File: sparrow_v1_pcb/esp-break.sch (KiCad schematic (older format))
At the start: 23 parts, among them J1 Conn_02x03_Odd_Even, Q1 BSS138, Q2 BSS138, SW1 SW_Push, U1 ESP32-WROOM-32D, U2 AP1117-33

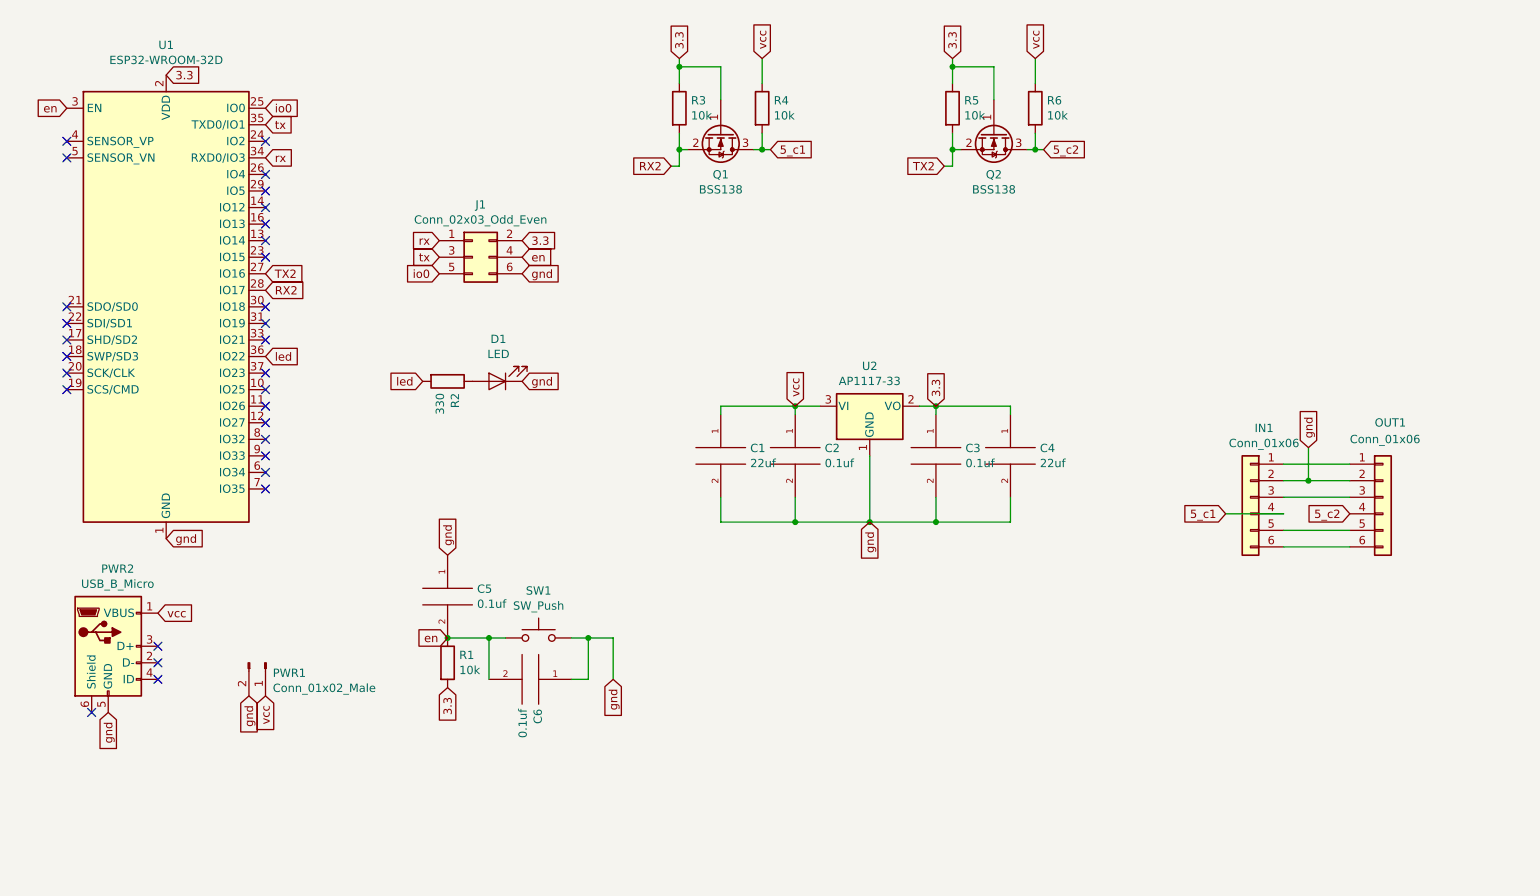
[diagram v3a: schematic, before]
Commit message: Added buck converter and routing
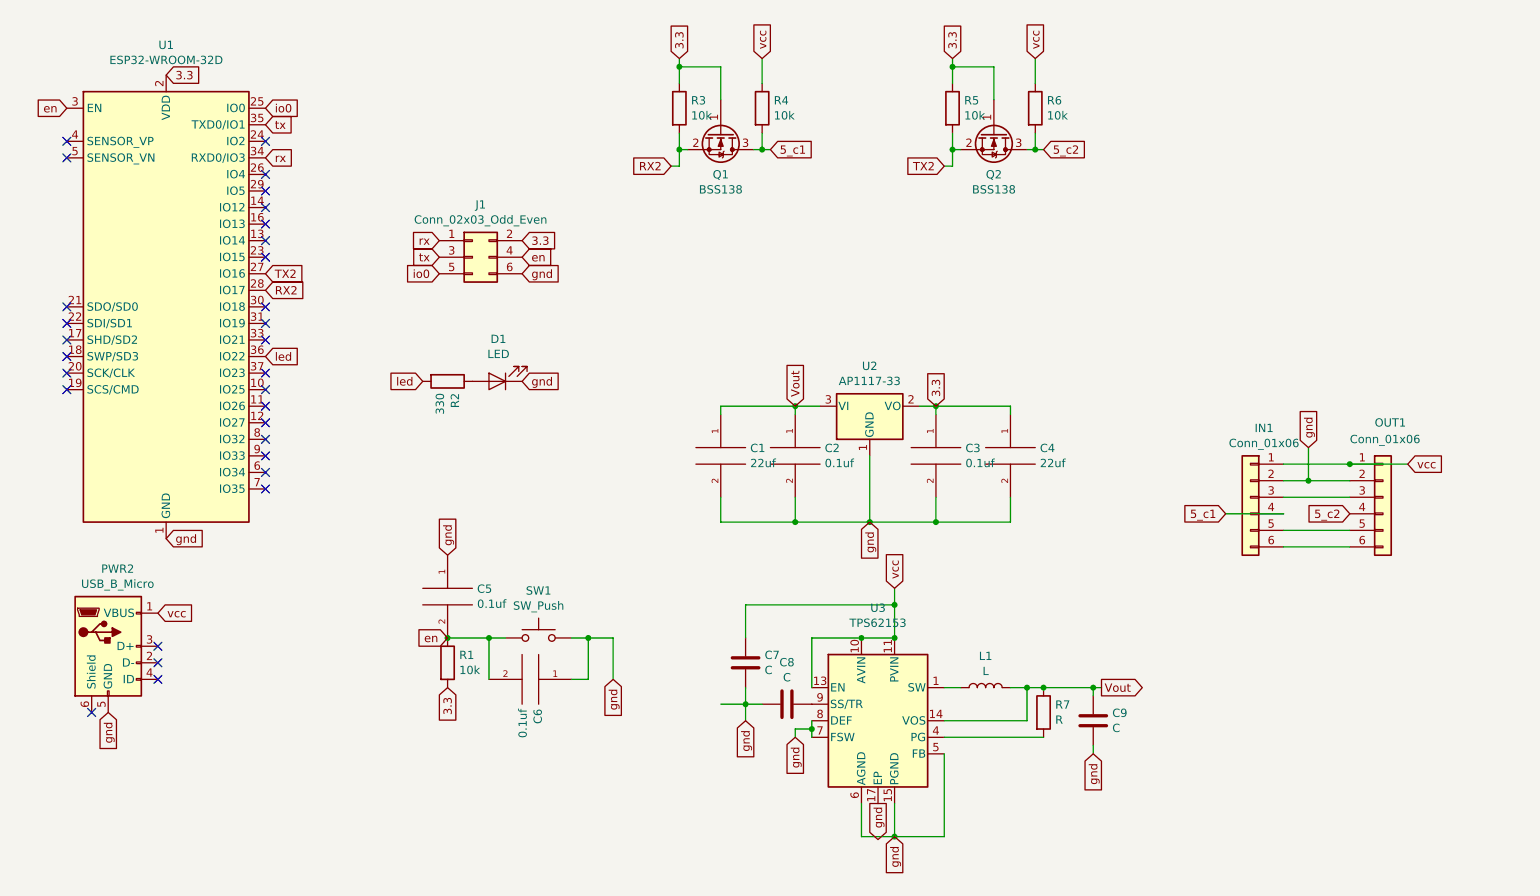
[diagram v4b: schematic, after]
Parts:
- removed PWR1: Conn_01x02_Male, Connector_PinHeader_2.54mm:PinHeader_1x02_P2.54mm_Vertical, symbol Connector:Conn_01x02_Male
- added C7: C, Capacitor_SMD:C_1210_3225Metric, symbol Device:C
- added C8: C, Capacitor_SMD:C_0201_0603Metric, symbol Device:C
- added C9: C, Capacitor_SMD:C_0805_2012Metric, symbol Device:C
- added L1: L, Inductor_SMD:L_Coilcraft_XxL4020, symbol Device:L
- added R7: R, Resistor_SMD:R_0603_1608Metric, symbol Device:R
- added U3: TPS62153, Package_DFN_QFN:VQFN-16-1EP_3x3mm_P0.5mm_EP1.68x1.68mm_ThermalVias, symbol Regulator_Switching:TPS62153
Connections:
- net gnd: now also C7.2, C8.2, C9.2, U3.15 (PGND), U3.16 (PGND), U3.17 (EP), U3.5 (FB), U3.6 (AGND), U3.7 (FSW), U3.8 (DEF)
- net vcc: now also IN1.1 (Pin_1), OUT1.1 (Pin_1), C7.1, U3.10 (AVIN), U3.11 (PVIN), U3.12 (PVIN), U3.13 (EN); no longer C1.1, C2.1, U2.3 (VI)
- new net: L1.1, U3.1 (SW), U3.2 (SW), U3.3 (SW)
- new net: R7.2, U3.4 (PG)
- new net: C8.1, U3.9 (SS/TR)
- new net Vout: C1.1, C2.1, C9.1, L1.2, R7.1, U2.3 (VI), U3.14 (VOS)
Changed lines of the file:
@@
 gnd
 Text GLabel 6400 2800 1    50   Input ~ 0
-vcc
+Vout
 Text GLabel 2600 800  2    50   Input ~ 0
 3.3
@@
 	9350 3350 9750 3350
 Text GLabel 9500 3050 1    50   Input ~ 0
-gnd
-$Comp
-L Connector:Conn_01x02_Male PWR1
-U 1 1 5DCB9F6F
-P 3200 4350
-F 0 "PWR1" V 3262 4394 50  0000 L CNN
-F 1 "Conn_01x02_Male" V 3353 4394 50  0000 L CNN
-F 2 "Connector_PinHeader_2.54mm:PinHeader_1x02_P2.54mm_Vertical" H 3200 4350 50  0001 C CNN
-F 3 "~" H 3200 4350 50  0001 C CNN
-	1    3200 4350
-	0    1    1    0
-$EndComp
-Text GLabel 3200 4550 3    50   Input ~ 0
-vcc
-Text GLabel 3100 4550 3    50   Input ~ 0
 gnd
 $Comp
@@
 NoConn ~ 2000 2600
 NoConn ~ 2000 2700
+$Comp
+L Regulator_Switching:TPS62153 U3
+U 1 1 5F00BF3A
+P 6900 4700
+F 0 "U3" H 6900 5381 50  0000 C CNN
+F 1 "TPS62153" H 6900 5290 50  0000 C CNN
+F 2 "Package_DFN_QFN:VQFN-16-1EP_3x3mm_P0.5mm_EP1.68x1.68mm_ThermalVias" H 7050 4250 50  0001 L CNN
+F 3 "http://www.ti.com/lit/ds/symlink/TPS62150.pdf" H 6900 4700 50  0001 C CNN
+	1    6900 4700
+	1    0    0    -1
+$EndComp
+Text GLabel 7000 3900 1    50   Input ~ 0
+vcc
+Wire Wire Line
+	6500 4500 6500 4200
+Wire Wire Line
+	6500 4200 6800 4200
+Wire Wire Line
+	6800 4200 7000 4200
+Connection ~ 6800 4200
+Wire Wire Line
+	7000 4200 7000 4000
+Connection ~ 7000 4200
+$Comp
+L Device:C C8
+U 1 1 5F0139AE
+P 6350 4600
+F 0 "C8" V 6098 4600 50  0000 C CNN
+F 1 "C" V 6189 4600 50  0000 C CNN
+F 2 "Capacitor_SMD:C_0201_0603Metric" H 6388 4450 50  0001 C CNN
+F 3 "~" H 6350 4600 50  0001 C CNN
+	1    6350 4600
+	0    1    1    0
+$EndComp
+Wire Wire Line
+	6200 4600 6100 4600
+Text GLabel 6100 4700 3    50   Input ~ 0
+gnd
+Wire Wire Line
+	6100 4700 6100 4600
+Connection ~ 6100 4600
+Wire Wire Line
+	6100 4600 5950 4600
+$Comp
+L Device:C C7
+U 1 1 5F0181AC
+P 6100 4350
+F 0 "C7" H 6215 4396 50  0000 L CNN
+F 1 "C" H 6215 4305 50  0000 L CNN
+F 2 "Capacitor_SMD:C_1210_3225Metric" H 6138 4200 50  0001 C CNN
+F 3 "~" H 6100 4350 50  0001 C CNN
+	1    6100 4350
+	1    0    0    -1
+$EndComp
+Wire Wire Line
+	6100 4500 6100 4600
+Wire Wire Line
+	6100 4200 6100 4000
+Wire Wire Line
+	6100 4000 7000 4000
+Connection ~ 7000 4000
+Wire Wire Line
+	7000 4000 7000 3900
+Wire Wire Line
+	6500 4700 6500 4750
+Wire Wire Line
+	6500 4750 6400 4750
+Wire Wire Line
+	6400 4750 6400 4800
+Connection ~ 6500 4750
+Wire Wire Line
+	6500 4750 6500 4800
+Text GLabel 6400 4800 3    50   Input ~ 0
+gnd
+Wire Wire Line
+	6800 5200 6800 5400
+Wire Wire Line
+	6800 5400 7000 5400
+Wire Wire Line
+	7000 5400 7000 5200
+Wire Wire Line
+	7300 4900 7300 5400
+Wire Wire Line
+	7300 5400 7000 5400
+Connection ~ 7000 5400
+Text GLabel 7000 5400 3    50   Input ~ 0
+gnd
+Wire Wire Line
+	7300 4700 7800 4700
+Wire Wire Line
+	7800 4700 7800 4500
+$Comp
+L Device:R R7
+U 1 1 5F02689D
+P 7900 4650
+F 0 "R7" H 7970 4696 50  0000 L CNN
+F 1 "R" H 7970 4605 50  0000 L CNN
+F 2 "Resistor_SMD:R_0603_1608Metric" V 7830 4650 50  0001 C CNN
+F 3 "~" H 7900 4650 50  0001 C CNN
+	1    7900 4650
+	1    0    0    -1
+$EndComp
+Wire Wire Line
+	7300 4800 7900 4800
+Wire Wire Line
+	7800 4500 7900 4500
+Wire Wire Line
+	7900 4500 8200 4500
+Connection ~ 7900 4500
+$Comp
+L Device:C C9
+U 1 1 5F02D11A
+P 8200 4700
+F 0 "C9" H 8315 4746 50  0000 L CNN
+F 1 "C" H 8315 4655 50  0000 L CNN
+F 2 "Capacitor_SMD:C_0805_2012Metric" H 8238 4550 50  0001 C CNN
+F 3 "~" H 8200 4700 50  0001 C CNN
+	1    8200 4700
+	1    0    0    -1
+$EndComp
+Wire Wire Line
+	8200 4500 8200 4550
+Text GLabel 8200 4900 3    50   Input ~ 0
+gnd
+Wire Wire Line
+	8200 4850 8200 4900
+$Comp
+L Device:L L1
+U 1 1 5F032225
+P 7550 4500
+F 0 "L1" V 7740 4500 50  0000 C CNN
+F 1 "L" V 7649 4500 50  0000 C CNN
+F 2 "Inductor_SMD:L_Coilcraft_XxL4020" H 7550 4500 50  0001 C CNN
+F 3 "~" H 7550 4500 50  0001 C CNN
+	1    7550 4500
+	0    -1   -1   0
+$EndComp
+Wire Wire Line
+	7300 4500 7400 4500
+Wire Wire Line
+	7700 4500 7800 4500
+Connection ~ 7800 4500
+Text GLabel 8250 4500 2    50   Output ~ 0
+Vout
+Wire Wire Line
+	8200 4500 8250 4500
+Connection ~ 8200 4500
+Text GLabel 6900 5200 3    50   Output ~ 0
+gnd
+Text GLabel 10100 3150 2    50   Input ~ 0
+vcc
+Wire Wire Line
+	9750 3150 10100 3150
+Connection ~ 9750 3150
 $EndSCHEMATC

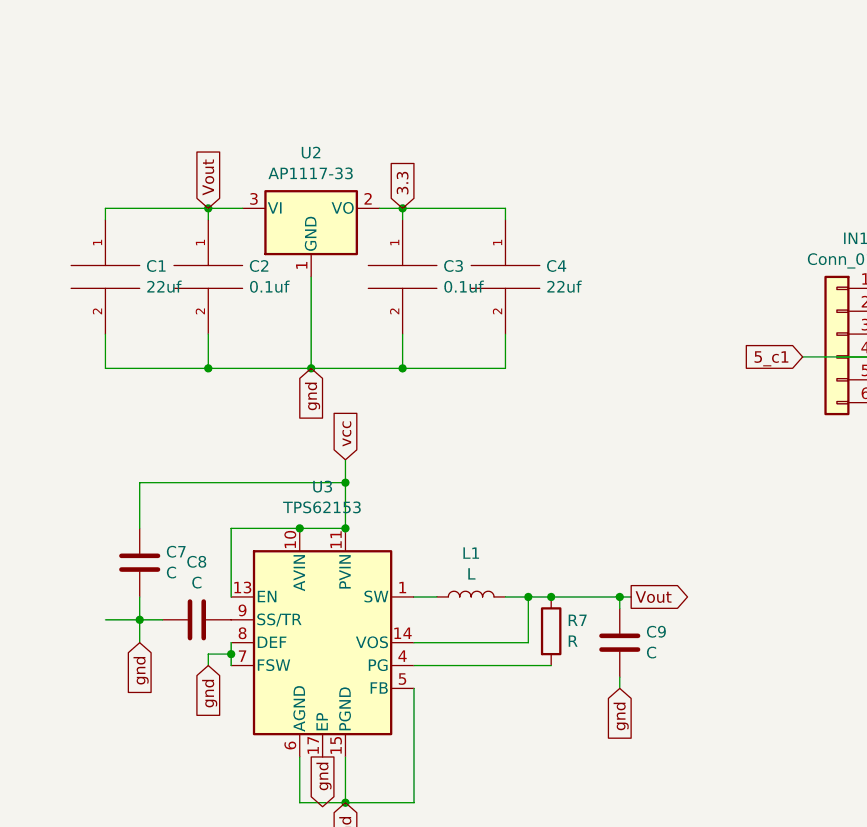
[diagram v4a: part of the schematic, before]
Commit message: added new component to schematic: LDO from ST
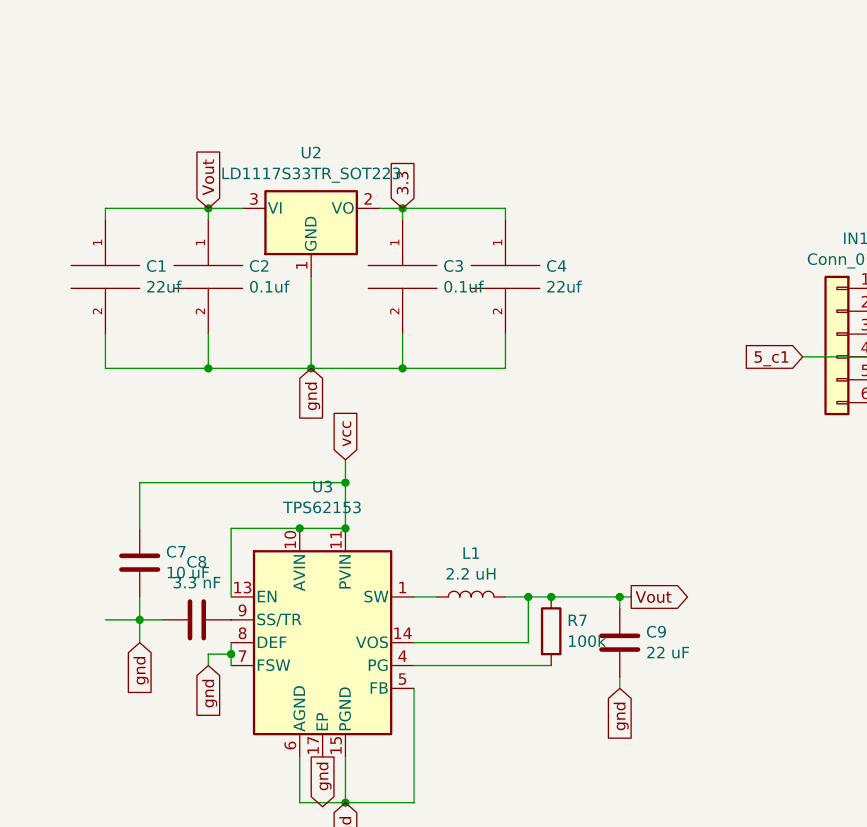
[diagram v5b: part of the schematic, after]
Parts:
- removed U2: AP1117-33, Package_TO_SOT_SMD:SOT-223-3_TabPin2, symbol Regulator_Linear:AP1117-33
- added U2: LD1117S33TR_SOT223, Package_TO_SOT_SMD:SOT-223-3_TabPin2, symbol Regulator_Linear:LD1117S33TR_SOT223
- C1, C2, C3, C4, C5, C6: footprint Capacitor_SMD:C_0201_0603Metric -> Capacitor_SMD:C_0402_1005Metric
- C7: value C -> 10 uF
- C8: value C -> 3.3 nF; footprint Capacitor_SMD:C_0201_0603Metric -> Capacitor_SMD:C_0402_1005Metric
- C9: value C -> 22 uF
- D1: footprint LED_SMD:LED_0201_0603Metric -> LED_SMD:LED_0402_1005Metric
- L1: value L -> 2.2 uH
- R7: value R -> 100k; footprint Resistor_SMD:R_0603_1608Metric -> Resistor_SMD:R_0201_0603Metric
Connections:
- net 3.3: now also U2.2 (VO)
- net Vout: now also U2.3 (VI)
- net gnd: now also U2.1 (GND)
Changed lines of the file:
@@
 	9750 3550 9350 3550
-$Comp
-L Regulator_Linear:AP1117-33 U2
-U 1 1 5DB9A6F8
-P 6850 2800
-F 0 "U2" H 6850 3042 50  0000 C CNN
-F 1 "AP1117-33" H 6850 2951 50  0000 C CNN
-F 2 "Package_TO_SOT_SMD:SOT-223-3_TabPin2" H 6850 3000 50  0001 C CNN
-F 3 "http://www.diodes.com/datasheets/AP1117.pdf" H 6950 2550 50  0001 C CNN
-	1    6850 2800
-	1    0    0    -1
-$EndComp
 $Comp
 L pspice:C C2
@@
 F 0 "C2" H 6578 3146 50  0000 L CNN
 F 1 "0.1uf" H 6578 3055 50  0000 L CNN
-F 2 "Capacitor_SMD:C_0201_0603Metric" H 6400 3100 50  0001 C CNN
+F 2 "Capacitor_SMD:C_0402_1005Metric" H 6400 3100 50  0001 C CNN
 F 3 "~" H 6400 3100 50  0001 C CNN
 	1    6400 3100
@@
 F 0 "C1" H 6128 3146 50  0000 L CNN
 F 1 "22uf" H 6128 3055 50  0000 L CNN
-F 2 "Capacitor_SMD:C_0201_0603Metric" H 5950 3100 50  0001 C CNN
+F 2 "Capacitor_SMD:C_0402_1005Metric" H 5950 3100 50  0001 C CNN
 F 3 "~" H 5950 3100 50  0001 C CNN
 	1    5950 3100
@@
 F 0 "C4" H 7878 3146 50  0000 L CNN
 F 1 "22uf" H 7878 3055 50  0000 L CNN
-F 2 "Capacitor_SMD:C_0201_0603Metric" H 7700 3100 50  0001 C CNN
+F 2 "Capacitor_SMD:C_0402_1005Metric" H 7700 3100 50  0001 C CNN
 F 3 "~" H 7700 3100 50  0001 C CNN
 	1    7700 3100
@@
 F 0 "C3" H 7428 3146 50  0000 L CNN
 F 1 "0.1uf" H 7428 3055 50  0000 L CNN
-F 2 "Capacitor_SMD:C_0201_0603Metric" H 7250 3100 50  0001 C CNN
+F 2 "Capacitor_SMD:C_0402_1005Metric" H 7250 3100 50  0001 C CNN
 F 3 "~" H 7250 3100 50  0001 C CNN
 	1    7250 3100
@@
 F 0 "D1" H 4593 2395 50  0000 C CNN
 F 1 "LED" H 4593 2486 50  0000 C CNN
-F 2 "LED_SMD:LED_0201_0603Metric" H 4600 2650 50  0001 C CNN
+F 2 "LED_SMD:LED_0402_1005Metric" H 4600 2650 50  0001 C CNN
 F 3 "~" H 4600 2650 50  0001 C CNN
 	1    4600 2650
@@
 F 0 "C5" H 4478 3996 50  0000 L CNN
 F 1 "0.1uf" H 4478 3905 50  0000 L CNN
-F 2 "Capacitor_SMD:C_0201_0603Metric" H 4300 3950 50  0001 C CNN
+F 2 "Capacitor_SMD:C_0402_1005Metric" H 4300 3950 50  0001 C CNN
 F 3 "~" H 4300 3950 50  0001 C CNN
 	1    4300 3950
@@
 F 0 "C6" H 4978 4496 50  0000 L CNN
 F 1 "0.1uf" H 4978 4405 50  0000 L CNN
-F 2 "Capacitor_SMD:C_0201_0603Metric" H 4800 4450 50  0001 C CNN
+F 2 "Capacitor_SMD:C_0402_1005Metric" H 4800 4450 50  0001 C CNN
 F 3 "~" H 4800 4450 50  0001 C CNN
 	1    4800 4450
@@
 P 6350 4600
 F 0 "C8" V 6098 4600 50  0000 C CNN
-F 1 "C" V 6189 4600 50  0000 C CNN
-F 2 "Capacitor_SMD:C_0201_0603Metric" H 6388 4450 50  0001 C CNN
+F 1 "3.3 nF" V 6189 4600 50  0000 C CNN
+F 2 "Capacitor_SMD:C_0402_1005Metric" H 6388 4450 50  0001 C CNN
 F 3 "~" H 6350 4600 50  0001 C CNN
 	1    6350 4600
@@
 P 6100 4350
 F 0 "C7" H 6215 4396 50  0000 L CNN
-F 1 "C" H 6215 4305 50  0000 L CNN
+F 1 "10 uF" H 6215 4305 50  0000 L CNN
 F 2 "Capacitor_SMD:C_1210_3225Metric" H 6138 4200 50  0001 C CNN
 F 3 "~" H 6100 4350 50  0001 C CNN
@@
 P 7900 4650
 F 0 "R7" H 7970 4696 50  0000 L CNN
-F 1 "R" H 7970 4605 50  0000 L CNN
-F 2 "Resistor_SMD:R_0603_1608Metric" V 7830 4650 50  0001 C CNN
+F 1 "100k" H 7970 4605 50  0000 L CNN
+F 2 "Resistor_SMD:R_0201_0603Metric" V 7830 4650 50  0001 C CNN
 F 3 "~" H 7900 4650 50  0001 C CNN
 	1    7900 4650
@@
 P 8200 4700
 F 0 "C9" H 8315 4746 50  0000 L CNN
-F 1 "C" H 8315 4655 50  0000 L CNN
+F 1 "22 uF" H 8315 4655 50  0000 L CNN
 F 2 "Capacitor_SMD:C_0805_2012Metric" H 8238 4550 50  0001 C CNN
 F 3 "~" H 8200 4700 50  0001 C CNN
@@
 P 7550 4500
 F 0 "L1" V 7740 4500 50  0000 C CNN
-F 1 "L" V 7649 4500 50  0000 C CNN
+F 1 "2.2 uH" V 7649 4500 50  0000 C CNN
 F 2 "Inductor_SMD:L_Coilcraft_XxL4020" H 7550 4500 50  0001 C CNN
 F 3 "~" H 7550 4500 50  0001 C CNN
@@
 	9750 3150 10100 3150
 Connection ~ 9750 3150
+$Comp
+L Regulator_Linear:LD1117S33TR_SOT223 U2
+U 1 1 5F0B3AAC
+P 6850 2800
+F 0 "U2" H 6850 3042 50  0000 C CNN
+F 1 "LD1117S33TR_SOT223" H 6850 2951 50  0000 C CNN
+F 2 "Package_TO_SOT_SMD:SOT-223-3_TabPin2" H 6850 3000 50  0001 C CNN
+F 3 "http://www.st.com/st-web-ui/static/active/en/resource/technical/document/datasheet/CD00000544.pdf" H 6950 2550 50  0001 C CNN
+	1    6850 2800
+	1    0    0    -1
+$EndComp
 $EndSCHEMATC
